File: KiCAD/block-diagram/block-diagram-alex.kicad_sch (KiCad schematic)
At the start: 33 parts, among them J1 Conn_01x08, J2 Conn_01x08, J3 Conn_01x10, Q3 NMOS, Q4 NMOS, U1 74LS02, U3 74LS11, U6 LMC555xM

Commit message: fix some connectors
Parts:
- J3: footprint Connector_PinSocket_2.54mm:PinSocket_1x10_P2.54mm_Vertical -> Connector_PinHeader_2.54mm:PinHeader_1x10_P2.54mm_Vertical
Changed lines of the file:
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@@
 			)
 		)
-		(property "Footprint" "Connector_PinSocket_2.54mm:PinSocket_1x10_P2.54mm_Vertical"
+		(property "Footprint" "Connector_PinHeader_2.54mm:PinHeader_1x10_P2.54mm_Vertical"
 			(at 144.78 170.18 0)
 			(effects

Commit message: Potentiometer
I added the potentiometer to modulate the watchdog time constant.
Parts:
- added RV1: R_Potentiometer_US, Potentiometer_THT:Potentiometer_ACP_CA6-H2,5_Horizontal, symbol Device:R_Potentiometer_US
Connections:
- net +5V: now also RV1.1; no longer R2.1
- net GND: now also RV1.2
- new net: R2.1, RV1.3
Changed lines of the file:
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@@
 	(wire
 		(pts
-			(xy 195.58 22.86) (xy 212.09 22.86)
+			(xy 195.58 22.86) (xy 200.66 22.86)
 		)
 		(stroke
@@
 	(wire
 		(pts
+			(xy 208.28 22.86) (xy 212.09 22.86)
+		)
+		(stroke
+			(width 0)
+			(type default)
+		)
+	)
+	(wire
+		(pts
 			(xy 176.53 38.1) (xy 182.88 38.1)
 		)
@@
 	(symbol
 		(lib_id "power:GND")
+		(at 204.47 19.05 180)
+		(unit 1)
+		(exclude_from_sim no)
+		(in_bom yes)
+		(on_board yes)
+		(dnp no)
+		(fields_autoplaced yes)
+		(property "Reference" "#PWR029"
+			(at 204.47 12.7 0)
+			(effects
+				(font
+					(size 1.27 1.27)
+				)
+				(hide yes)
+			)
+		)
+		(property "Value" "GND"
+			(at 204.47 13.97 0)
+			(effects
+				(font
+					(size 1.27 1.27)
+				)
+			)
+		)
+		(property "Footprint" ""
+			(at 204.47 19.05 0)
+			(effects
+				(font
+					(size 1.27 1.27)
+				)
+				(hide yes)
+			)
+		)
+		(property "Datasheet" ""
+			(at 204.47 19.05 0)
+			(effects
+				(font
+					(size 1.27 1.27)
+				)
+				(hide yes)
+			)
+		)
+		(property "Description" "Power symbol creates a global label with name \"GND\" , ground"
+			(at 204.47 19.05 0)
+			(effects
+				(font
+					(size 1.27 1.27)
+				)
+				(hide yes)
+			)
+		)
+		(pin "1"
+		)
+		(instances
+			(project "block-diagram-alex"
+				(path "/db38bfac-663c-442a-8ac2-f7bf1aa9a3fd"
+					(reference "#PWR029")
+					(unit 1)
+				)
+			)
+		)
+	)
+	(symbol
+		(lib_id "power:GND")
 		(at 185.42 132.08 0)
 		(unit 1)
@@
 					(unit 1)
 				)
+			)
+		)
+	)
+	(symbol
+		(lib_id "Device:R_Potentiometer_US")
+		(at 204.47 22.86 90)
+		(unit 1)
+		(exclude_from_sim no)
+		(in_bom yes)
+		(on_board yes)
+		(dnp no)
+		(fields_autoplaced yes)
+		(property "Reference" "RV1"
+			(at 204.47 26.67 90)
+			(effects
+				(font
+					(size 1.27 1.27)
+				)
+			)
+		)
+		(property "Value" "R_Potentiometer_US"
+			(at 204.47 29.21 90)
+			(effects
+				(font
+					(size 1.27 1.27)
+				)
+			)
+		)
+		(property "Footprint" "Potentiometer_THT:Potentiometer_ACP_CA6-H2,5_Horizontal"
+			(at 204.47 22.86 0)
+			(effects
+				(font
+					(size 1.27 1.27)
+				)
+				(hide yes)
+			)
+		)
+		(property "Datasheet" "~"
+			(at 204.47 22.86 0)
+			(effects
+				(font
+					(size 1.27 1.27)
+				)
+				(hide yes)
+			)
+		)
+		(property "Description" "Potentiometer, US symbol"
+			(at 204.47 22.86 0)
+			(effects
+				(font
+					(size 1.27 1.27)
+				)
+				(hide yes)
+			)
+		)
+		(pin "2"
+		)
+		(pin "1"
+		)
+		(pin "3"
+		)
+		(instances
+			(project "block-diagram-alex"
+				(path "/db38bfac-663c-442a-8ac2-f7bf1aa9a3fd"
+					(reference "RV1")
+					(unit 1)
+				)

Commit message: Fix potentiometer
Corrected wiring for potentiometer
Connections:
- net +5V: now also RV1.2
- net GND: no longer RV1.2
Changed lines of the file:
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@@
 	(paper "A4")
+	(junction
+		(at 198.12 22.86)
+		(diameter 0)
+		(color 0 0 0 0)
+	)
 	(junction
 		(at 212.09 116.84)
@@
 	(wire
 		(pts
-			(xy 195.58 22.86) (xy 200.66 22.86)
+			(xy 195.58 22.86) (xy 198.12 22.86)
 		)
 		(stroke
@@
 	(wire
 		(pts
+			(xy 198.12 19.05) (xy 198.12 22.86)
+		)
+		(stroke
+			(width 0)
+			(type default)
+		)
+	)
+	(wire
+		(pts
 			(xy 212.09 22.86) (xy 212.09 26.67)
 		)
@@
 	(wire
 		(pts
+			(xy 204.47 19.05) (xy 198.12 19.05)
+		)
+		(stroke
+			(width 0)
+			(type default)
+		)
+	)
+	(wire
+		(pts
 			(xy 170.18 59.69) (xy 190.5 59.69)
 		)
@@
 		(pts
 			(xy 127 168.91) (xy 127 167.64)
+		)
+		(stroke
+			(width 0)
+			(type default)
+		)
+	)
+	(wire
+		(pts
+			(xy 198.12 22.86) (xy 200.66 22.86)
 		)
 		(stroke
@@
 					(unit 1)
 				)
-			)
-		)
-	)
-	(symbol
-		(lib_id "power:GND")
-		(at 204.47 19.05 180)
-		(unit 1)
-		(exclude_from_sim no)
-		(in_bom yes)
-		(on_board yes)
-		(dnp no)
-		(fields_autoplaced yes)
-		(property "Reference" "#PWR029"
-			(at 204.47 12.7 0)
-			(effects
-				(font
-					(size 1.27 1.27)
-				)
-				(hide yes)
-			)
-		)
-		(property "Value" "GND"
-			(at 204.47 13.97 0)
-			(effects
-				(font
-					(size 1.27 1.27)
-				)
-			)
-		)
-		(property "Footprint" ""
-			(at 204.47 19.05 0)
-			(effects
-				(font
-					(size 1.27 1.27)
-				)
-				(hide yes)
-			)
-		)
-		(property "Datasheet" ""
-			(at 204.47 19.05 0)
-			(effects
-				(font
-					(size 1.27 1.27)
-				)
-				(hide yes)
-			)
-		)
-		(property "Description" "Power symbol creates a global label with name \"GND\" , ground"
-			(at 204.47 19.05 0)
-			(effects
-				(font
-					(size 1.27 1.27)
-				)
-				(hide yes)
-			)
-		)
-		(pin "1"
-		)
-		(instances
-			(project "block-diagram-alex"
-				(path "/db38bfac-663c-442a-8ac2-f7bf1aa9a3fd"
-					(reference "#PWR029")
-					(unit 1)
-				)

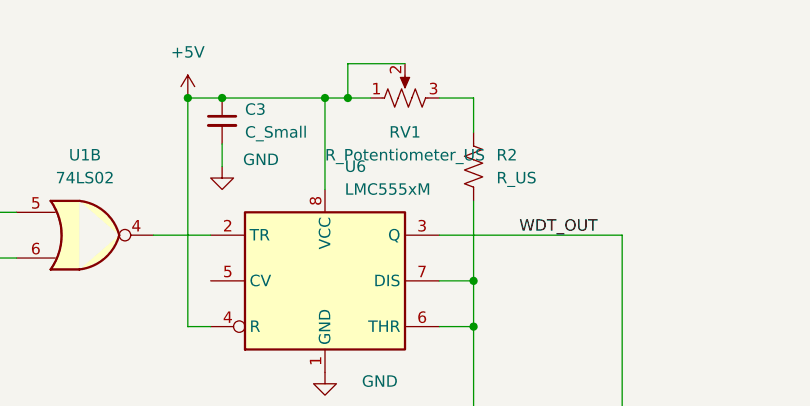
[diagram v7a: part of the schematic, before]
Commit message: Fix pot in schematic
rotated the potentiometer in the schematic to be the correct orientation so that it has the correct connections
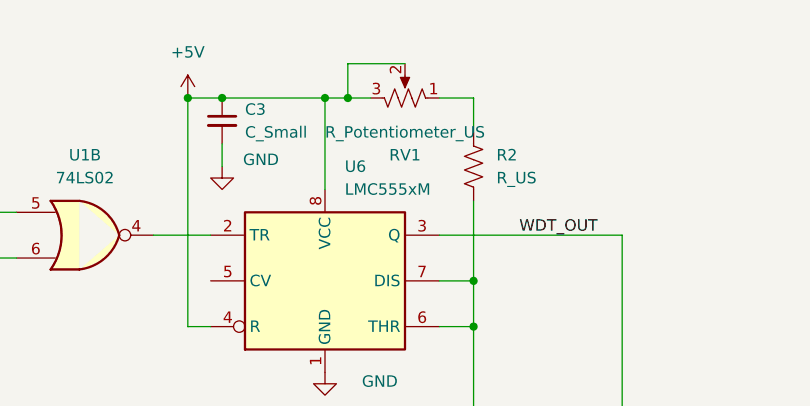
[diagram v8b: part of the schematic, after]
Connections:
- net +5V: now also RV1.3; no longer RV1.1
- net at R2.1: now also RV1.1; no longer RV1.3
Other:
- moved on the sheet: RV1
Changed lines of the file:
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@@
 	(symbol
 		(lib_id "Device:R_Potentiometer_US")
-		(at 204.47 22.86 90)
+		(at 204.47 22.86 270)
+		(mirror x)
 		(unit 1)
 		(exclude_from_sim no)
@@
 		(on_board yes)
 		(dnp no)
-		(fields_autoplaced yes)
 		(property "Reference" "RV1"
-			(at 204.47 26.67 90)
+			(at 204.47 29.21 90)
 			(effects
 				(font
@@
 		)
 		(property "Value" "R_Potentiometer_US"
-			(at 204.47 29.21 90)
+			(at 204.47 26.67 90)
 			(effects
 				(font
